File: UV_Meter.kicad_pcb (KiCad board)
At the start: 2 copper layers, 58.4 x 17.8 mm, 10 parts, among them SW1 SW_Push, U1 ATtiny85-20PU

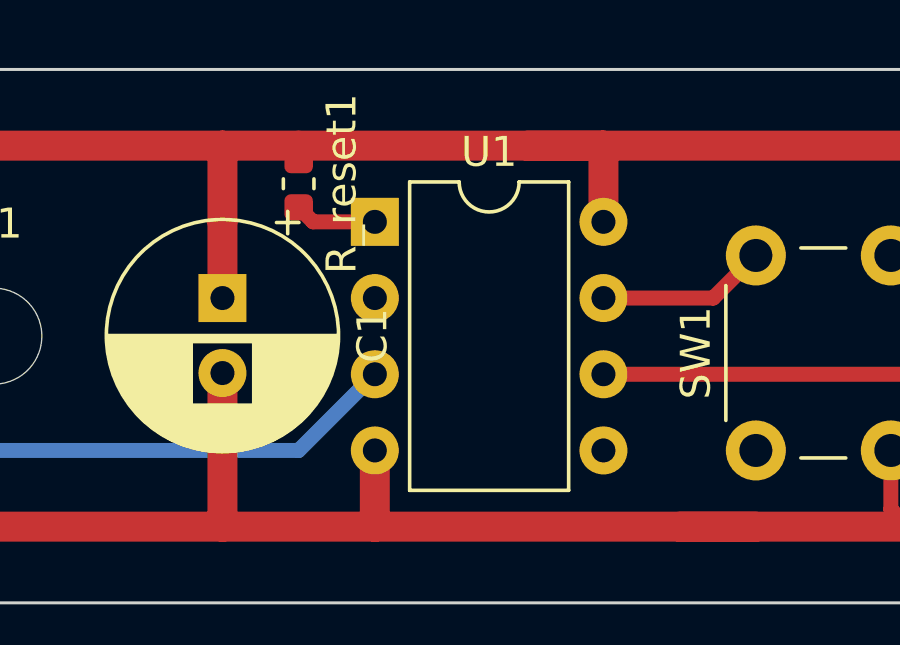
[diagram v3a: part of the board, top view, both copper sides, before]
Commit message: added 100nF ceramic, streamlined reset
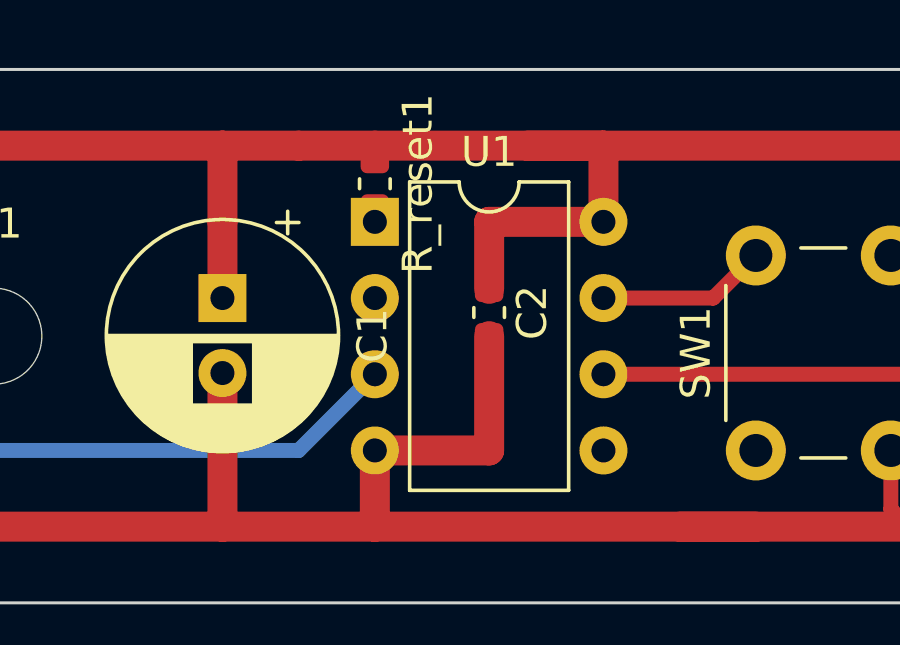
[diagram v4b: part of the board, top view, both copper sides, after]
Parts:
- added C2: 100nF, Capacitor_SMD:C_0603_1608Metric, F.Cu at (52.1, 28.4)
- C1: value 100u -> 100uF
- moved R_reset1 2.54 mm to (48.3, 24.1)
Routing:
- net GND: track 79.0 -> 86.6 mm
- net +5V: track 70.2 -> 76.2 mm
- net /reset: track 2.74 -> 0.48 mm
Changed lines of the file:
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@@
     (thickness 1.6)
     (drawings 6)
-    (tracks 45)
+    (tracks 49)
     (zones 0)
-    (modules 10)
+    (modules 11)
     (nets 9)
   )
@@
   )
   (setup
-    (last_trace_width 0.25)
+    (last_trace_width 1)
     (user_trace_width 0.25)
     (user_trace_width 0.5)
@@
     (add_net GND)
   )
+  (module Capacitor_SMD:C_0603_1608Metric (layer F.Cu)
+    (at 52.07 28.4225 270)
+    (descr "Capacitor SMD 0603 (1608 Metric), square (rectangular) end terminal, IPC_7351 nominal, (Body size source: http://www.tortai-tech.com/upload/download/2011102023233369053.pdf), generated with kicad-footprint-generator")
+    (tags capacitor)
+    (attr smd)
+    (fp_text reference C2 (at 0 -1.43 270) (layer F.SilkS)
+      (effects (font (size 1 1) (thickness 0.15)))
+    )
+    (fp_text value 100nF (at 0 1.43 270) (layer F.Fab)
+      (effects (font (size 1 1) (thickness 0.15)))
+    )
+    (fp_text user %R (at 0 0 270) (layer F.Fab)
+      (effects (font (size 0.4 0.4) (thickness 0.06)))
+    )
+    (fp_line (start 1.48 0.73) (end -1.48 0.73) (layer F.CrtYd) (width 0.05))
+    (fp_line (start 1.48 -0.73) (end 1.48 0.73) (layer F.CrtYd) (width 0.05))
+    (fp_line (start -1.48 -0.73) (end 1.48 -0.73) (layer F.CrtYd) (width 0.05))
+    (fp_line (start -1.48 0.73) (end -1.48 -0.73) (layer F.CrtYd) (width 0.05))
+    (fp_line (start -0.162779 0.51) (end 0.162779 0.51) (layer F.SilkS) (width 0.12))
+    (fp_line (start -0.162779 -0.51) (end 0.162779 -0.51) (layer F.SilkS) (width 0.12))
+    (fp_line (start 0.8 0.4) (end -0.8 0.4) (layer F.Fab) (width 0.1))
+    (fp_line (start 0.8 -0.4) (end 0.8 0.4) (layer F.Fab) (width 0.1))
+    (fp_line (start -0.8 -0.4) (end 0.8 -0.4) (layer F.Fab) (width 0.1))
+    (fp_line (start -0.8 0.4) (end -0.8 -0.4) (layer F.Fab) (width 0.1))
+    (pad 2 smd roundrect (at 0.7875 0 270) (size 0.875 0.95) (layers F.Cu F.Paste F.Mask) (roundrect_rratio 0.25)
+      (net 1 GND))
+    (pad 1 smd roundrect (at -0.7875 0 270) (size 0.875 0.95) (layers F.Cu F.Paste F.Mask) (roundrect_rratio 0.25)
+      (net 2 +5V))
+    (model ${KISYS3DMOD}/Capacitor_SMD.3dshapes/C_0603_1608Metric.wrl
+      (at (xyz 0 0 0))
+      (scale (xyz 1 1 1))
+      (rotate (xyz 0 0 0))
+    )
+  )
   (module MountingHole:MountingHole_3.2mm_M3_ISO14580 (layer F.Cu)
     (at 35.56 29.21)
@@
   )
   (module Resistor_SMD:R_0603_1608Metric (layer F.Cu)
-    (at 45.72 24.13 270)
+    (at 48.26 24.13 270)
     (descr "Resistor SMD 0603 (1608 Metric), square (rectangular) end terminal, IPC_7351 nominal, (Body size source: http://www.tortai-tech.com/upload/download/2011102023233369053.pdf), generated with kicad-footprint-generator")
     (tags resistor)
@@
       (effects (font (size 1 1) (thickness 0.15)))
     )
-    (fp_text value 100u (at 1.25 5 270) (layer F.Fab)
+    (fp_text value 100uF (at 1.25 5 270) (layer F.Fab)
       (effects (font (size 1 1) (thickness 0.15)))
     )
@@
   (segment (start 65.46 33.02) (end 65.46 34.98) (width 0.5) (layer F.Cu) (net 1))
   (segment (start 65.46 34.98) (end 66.04 35.56) (width 0.5) (layer F.Cu) (net 1))
+  (segment (start 52.07 33.02) (end 48.26 33.02) (width 1) (layer F.Cu) (net 1))
+  (segment (start 52.07 33.02) (end 52.07 29.21) (width 1) (layer F.Cu) (net 1))
   (segment (start 55.88 25.4) (end 55.88 22.86) (width 1) (layer F.Cu) (net 2))
   (segment (start 71.12 22.86) (end 53.34 22.86) (width 1) (layer F.Cu) (net 2))
@@
   (segment (start 43.18 27.94) (end 43.18 25.4) (width 1) (layer F.Cu) (net 2))
   (segment (start 43.18 25.4) (end 43.18 22.86) (width 1) (layer F.Cu) (net 2))
-  (segment (start 45.72 23.3425) (end 45.72 22.86) (width 0.5) (layer F.Cu) (net 2))
-  (segment (start 55.88 22.86) (end 45.72 22.86) (width 1) (layer F.Cu) (net 2))
   (segment (start 45.72 22.86) (end 43.18 22.86) (width 1) (layer F.Cu) (net 2))
+  (segment (start 55.88 25.4) (end 52.07 25.4) (width 1) (layer F.Cu) (net 2))
+  (segment (start 48.26 23.3425) (end 48.26 22.86) (width 0.5) (layer F.Cu) (net 2))
+  (segment (start 55.88 22.86) (end 48.26 22.86) (width 1) (layer F.Cu) (net 2))
+  (segment (start 48.26 22.86) (end 45.72 22.86) (width 1) (layer F.Cu) (net 2))
+  (segment (start 52.07 25.4) (end 52.07 27.635) (width 1) (layer F.Cu) (net 2))
   (segment (start 55.88 30.48) (end 67.7925 30.48) (width 0.5) (layer F.Cu) (net 3))
   (segment (start 59.54 27.94) (end 60.96 26.52) (width 0.5) (layer F.Cu) (net 4))
@@
   (segment (start 72.470001 31.830001) (end 77.389999 31.830001) (width 0.5) (layer B.Cu) (net 7))
   (segment (start 71.12 30.48) (end 72.470001 31.830001) (width 0.5) (layer B.Cu) (net 7))
-  (segment (start 46.2025 25.4) (end 45.72 24.9175) (width 0.5) (layer F.Cu) (net 8))
-  (segment (start 48.26 25.4) (end 46.2025 25.4) (width 0.5) (layer F.Cu) (net 8))
+  (segment (start 48.26 24.9175) (end 48.26 25.4) (width 0.5) (layer F.Cu) (net 8))
   (zone (net 0) (net_name "") (layer F.Cu) (hatch edge 0.508)
     (connect_pads (clearance 0.508))

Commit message: added version, name; improved connector to horizontal
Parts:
- Audio1: footprint Connector_PinSocket_2.54mm:PinSocket_1x03_P2.54mm_Vertical -> Connector_PinSocket_2.54mm:PinSocket_1x03_P2.54mm_Horizontal
- C1: footprint Capacitor_THT:CP_Radial_D7.5mm_P2.50mm -> Capacitor_THT:CP_Radial_D5.0mm_P2.50mm
- F_LED1: value 500mA -> 1A
- moved C2 6.40 mm to (45.7, 29.2)
- moved Audio1 5.08 mm to (25.4, 27.9), turned to 0 degrees
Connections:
- Audio1 pad 1: /AO -> +5V
- Audio1 pad 3: +5V -> /line
- U1 pad 3: /AO -> /line
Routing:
- net /line: track 0.00 -> 23.9 mm
- net /AO: track 23.9 -> 0.00 mm
- net GND: track 86.6 -> 82.0 mm
- net +5V: track 76.2 -> 73.2 mm
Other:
- board text added: "Logo, version, label"
- board text added: "Remove Hole -> save 10 mm (fits on default perfboard!), save 2 LEDs; reduces size of C"
- board text added: "UV-Meter"
- board text added: "v2019/04/27"

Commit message: noted wrong polarity, moved SMD to backside
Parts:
- C1: footprint Capacitor_THT:CP_Radial_D5.0mm_P2.50mm -> Capacitor_THT:CP_Radial_D4.0mm_P2.00mm
- C2, R_data1, R_reset1: moved to B.Cu
- moved R_data1 10.2 mm to (58.4, 30.5)
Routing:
- net /r_data: track 10.5 -> 20.7 mm, vias 1 -> 0
- net /data: track 11.9 -> 1.75 mm
- net +5V: vias 0 -> 1
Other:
- board text added: "WRONG POLARITY!"
- board text added: "v2019/04/28"
- board text removed: "Logo, version, label"
- board text removed: "v2019/04/27"
